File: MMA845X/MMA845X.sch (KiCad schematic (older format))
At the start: 20 parts, among them J1 Conn_01x06, J2 Conn_01x04, J3 Conn_01x06, J4 Conn_01x04, Q2 BSS138DW, U1 AP2127K-3.3, U2 MMA8451

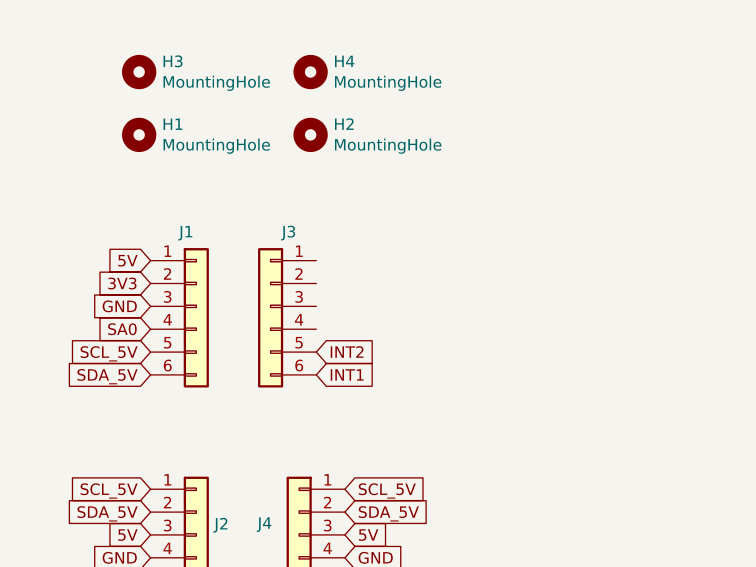
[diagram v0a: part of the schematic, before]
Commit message: MMA845X PCB and SCH edit
Extra Power Pins Added
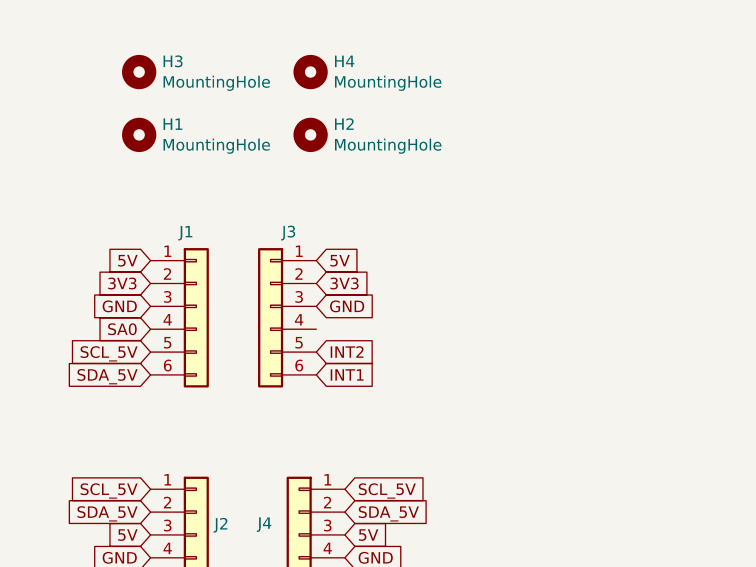
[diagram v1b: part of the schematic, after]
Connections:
- net 3V3: now also J3.2 (Pin_2)
- net 5V: now also J3.1 (Pin_1)
- net GND: now also J3.3 (Pin_3)
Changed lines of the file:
@@
 Text GLabel 1250 3925 0    50   Input ~ 0
 SA0
+Text GLabel 1975 3725 2    50   Input ~ 0
+3V3
+Text GLabel 1975 3625 2    50   Input ~ 0
+5V
+Text GLabel 1975 3825 2    50   Input ~ 0
+GND
 $EndSCHEMATC

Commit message: Part Numbers Added
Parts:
- U2: Part C118083 -> C118083, C11360, C122561
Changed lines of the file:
@@
 F 1 "MMA8451" H 5700 3498 50  0000 C CNN
 F 2 "SirBoardLibrary:QFN-COL-16-P=0.5" H 5700 3550 50  0001 C CNN
-F 3 "" H 5700 3550 50  0001 C CNN
-F 4 "C118083" H 5700 3475 50  0001 C CNN "Part"
+F 3 "https://datasheet.lcsc.com/szlcsc/Freescale-Semicon-MMA8452QR1_C11360.pdf" H 5700 3550 50  0001 C CNN
+F 4 "C118083, C11360, C122561" H 5700 3475 50  0001 C CNN "Part"
 	1    5700 3000
 	1    0    0    -1

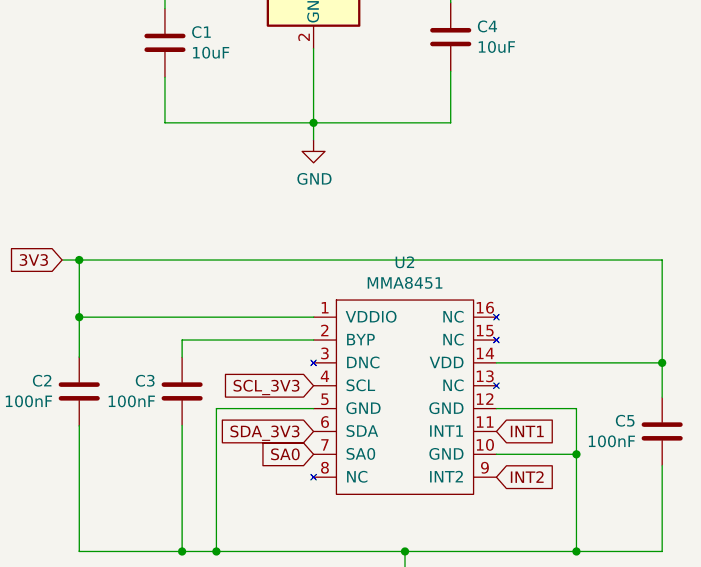
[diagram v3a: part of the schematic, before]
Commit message: Schematic and 3D render updates
Multiple boards
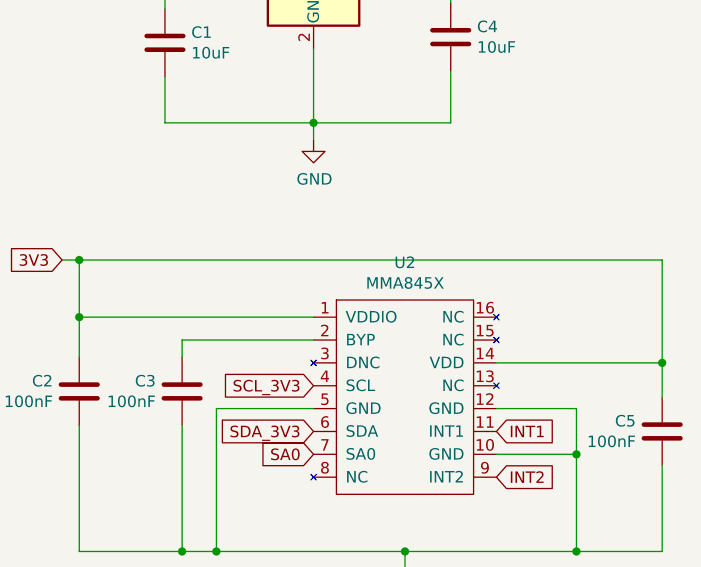
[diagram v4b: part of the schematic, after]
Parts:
- U2: value MMA8451 -> MMA845X
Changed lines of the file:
@@
 P 5700 3000
 F 0 "U2" H 5700 3588 50  0000 C CNN
-F 1 "MMA8451" H 5700 3498 50  0000 C CNN
+F 1 "MMA845X" H 5700 3498 50  0000 C CNN
 F 2 "SirBoardLibrary:QFN-COL-16-P=0.5" H 5700 3550 50  0001 C CNN
 F 3 "https://datasheet.lcsc.com/szlcsc/Freescale-Semicon-MMA8452QR1_C11360.pdf" H 5700 3550 50  0001 C CNN
